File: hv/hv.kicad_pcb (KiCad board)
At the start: 2 copper layers, 50 x 50 mm, 26 parts, among them P1 CONN_02X03, P10 CONN_01X01, P2 CONN_01X02, P3 CONN_01X01, P4 CONN_01X01, P5 CONN_01X01, P6 CONN_01X02, P7 CONN_01X01, P8 CONN_01X01, P9 CONN_01X01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

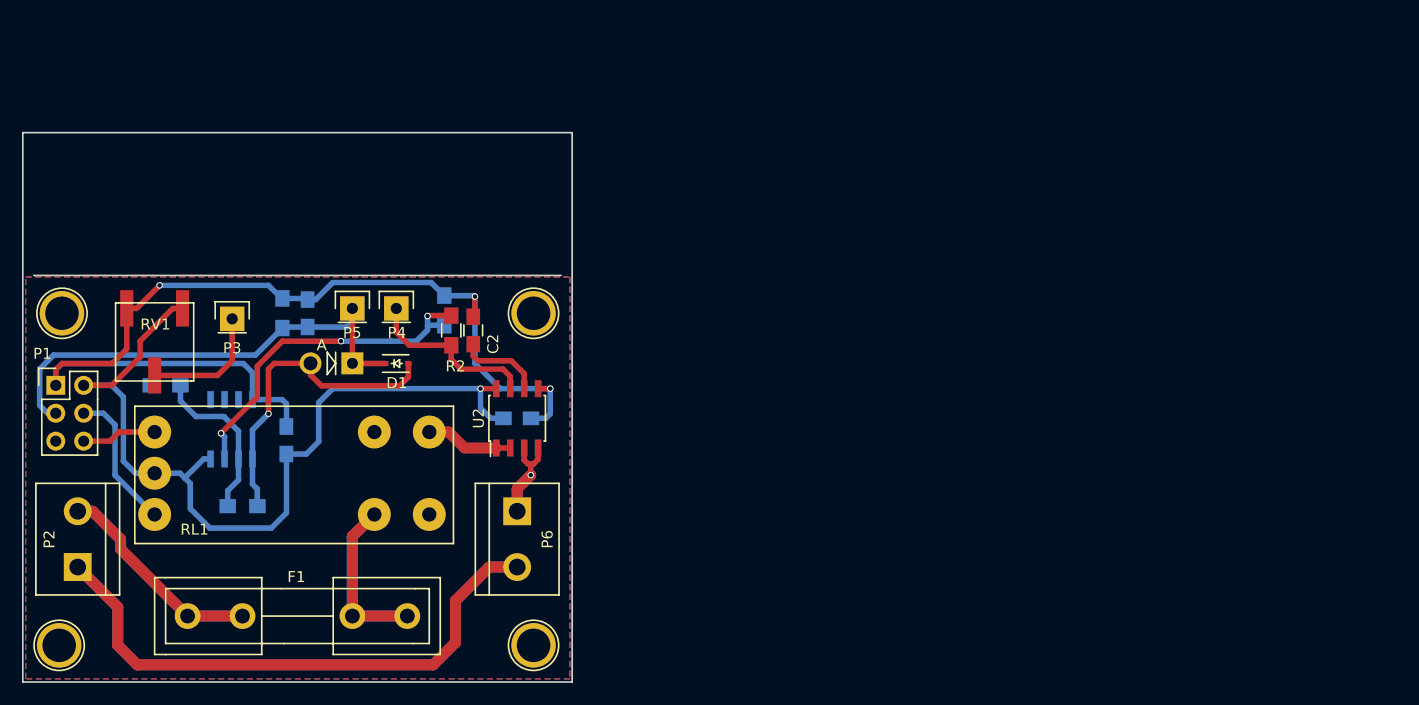
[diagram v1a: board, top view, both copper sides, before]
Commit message: Rerouting on 5x5 cm2
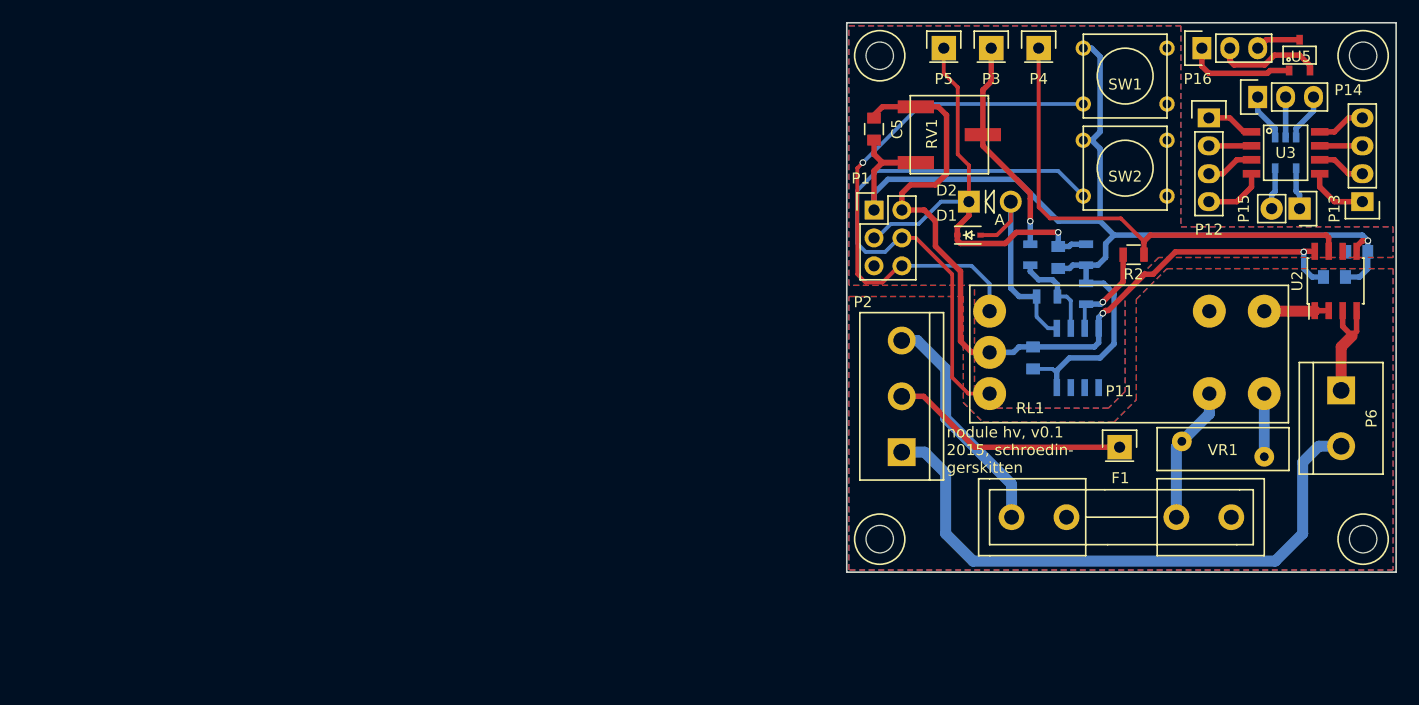
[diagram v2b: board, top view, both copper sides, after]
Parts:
- removed 1N4148: D, Diodes_ThroughHole:Diode_DO-41_SOD81_Vertical_AnodeUp
- added C5: C, Capacitors_SMD:C_0805, F.Cu at (157.5, 74.7)
- added D2: 1N148, Diodes_ThroughHole:Diode_DO-41_SOD81_Vertical_AnodeUp, F.Cu at (166.1, 81.3)
- added P11: CONN_01X01, Pin_Headers:Pin_Header_Straight_1x01, F.Cu at (179.8, 103.6)
- added P12: CONN_01X04, Pin_Headers:Pin_Header_Straight_1x04, F.Cu at (188.0, 73.7)
- added P13: CONN_01X04, Pin_Headers:Pin_Header_Straight_1x04, F.Cu at (201.9, 81.3)
- added P14: CONN_01X03, Pin_Headers:Pin_Header_Straight_1x03, F.Cu at (192.4, 71.8)
- added P15: CONN_01X02, Pin_Headers:Pin_Header_Straight_1x02, F.Cu at (196.2, 81.9)
- added P16: CONN_01X03, Pin_Headers:Pin_Header_Straight_1x03, F.Cu at (187.3, 67.3)
- added SW1: SW_PUSH, Buttons_Switches_ThroughHole:SW_PUSH_SMALL, F.Cu at (180.3, 69.8)
- added SW2: SW_PUSH, Buttons_Switches_ThroughHole:SW_PUSH_SMALL, F.Cu at (180.3, 78.2)
- added U3: dummy-8, SMD:SOIC_08_4.0mm_5.0mm_1.27mm, F.Cu at (194.9, 76.8)
- added U4: dummy-5, SMD:SOT-23-5, B.Cu at (194.9, 76.8)
- added U5: dummy-3, SMD:SOT-23-3, F.Cu at (196.2, 67.9)
- added VR1: VR, Varistors:RV_Disc_D12_W3.9_P7.5, F.Cu at (193.0, 104.5)
- C1, C3, C4: footprint Capacitors_SMD:C_0805_HandSoldering -> Capacitors_SMD:C_0805
- C2: footprint Capacitors_SMD:C_0805_HandSoldering -> Capacitors_SMD:C_0805; moved to B.Cu
- P2: value CONN_01X02 -> CONN_01X03; footprint Connect:bornier2 -> Connect:bornier3
- R1, R2, R3, R4, R5: footprint Resistors_SMD:R_0805_HandSoldering -> Resistors_SMD:R_0805
- moved C2 80.7 mm to (201.4, 85.9), turned to 0 degrees
- moved R1 79.6 mm to (171.7, 86.1), turned to 90 degrees
- moved P9 79.1 mm to (202.0, 68.0)
- moved P8 78.0 mm to (158.0, 68.0)
- moved U1 77.3 mm to (176.0, 95.5), turned to 270 degrees
- moved RL1 76.8 mm to (168.0, 95.0)
- moved P1 76.2 mm to (157.5, 82.0)
- moved P10 76.1 mm to (202.0, 112.0)
- moved P2 76.1 mm to (160.0, 99.0)
- moved P6 75.8 mm to (200.0, 101.0)
- moved R4 75.7 mm to (173.2, 89.9), turned to 180 degrees
- moved U2 75.5 mm to (199.5, 88.5)
- moved F1 75.5 mm to (180.0, 110.0)
- moved C4 75.5 mm to (199.4, 88.1)
- moved P7 75.3 mm to (158.0, 112.0)
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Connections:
- P2 pad 2: L -> Earth
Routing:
- net N: track 103.3 -> 55.5 mm
- net S: track 6.80 -> 48.8 mm, vias 0 -> 1
- net R: track 13.0 -> 51.3 mm
- net VSEN: track 16.1 -> 46.9 mm
- net Net-(R2-Pad1): track 31.8 -> 8.93 mm, vias 3 -> 1
- net Earth: track 0.00 -> 21.8 mm
- net GND: track 95.4 -> 116.3 mm, vias 3 -> 1
- net L: track 39.4 -> 21.1 mm
- net Net-(F1-Pad1): track 30.2 -> 12.5 mm
- net Net-(P16-Pad1): track 0.00 -> 9.96 mm
- net Net-(P16-Pad2): track 0.00 -> 9.81 mm
- net Net-(D1-Pad2): track 29.2 -> 19.7 mm, vias 1 -> 0
- net Net-(P3-Pad1): track 11.4 -> 20.0 mm, vias 0 -> 1
- net Net-(C2-Pad1): track 7.76 -> 0.00 mm
- net +5V: track 78.2 -> 85.4 mm, vias 1 -> 2
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- added copper zone on B.Cu, net Earth
- added copper zone on F.Cu, net Earth
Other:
- outline, holes or cut-outs redrawn
- net class Default: trace_width 1 -> 0.5
- board text added: "nodule hv, v0.1 2015, schroedin- gerskitten"
